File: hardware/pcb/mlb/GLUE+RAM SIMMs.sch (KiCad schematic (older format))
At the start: 15 parts

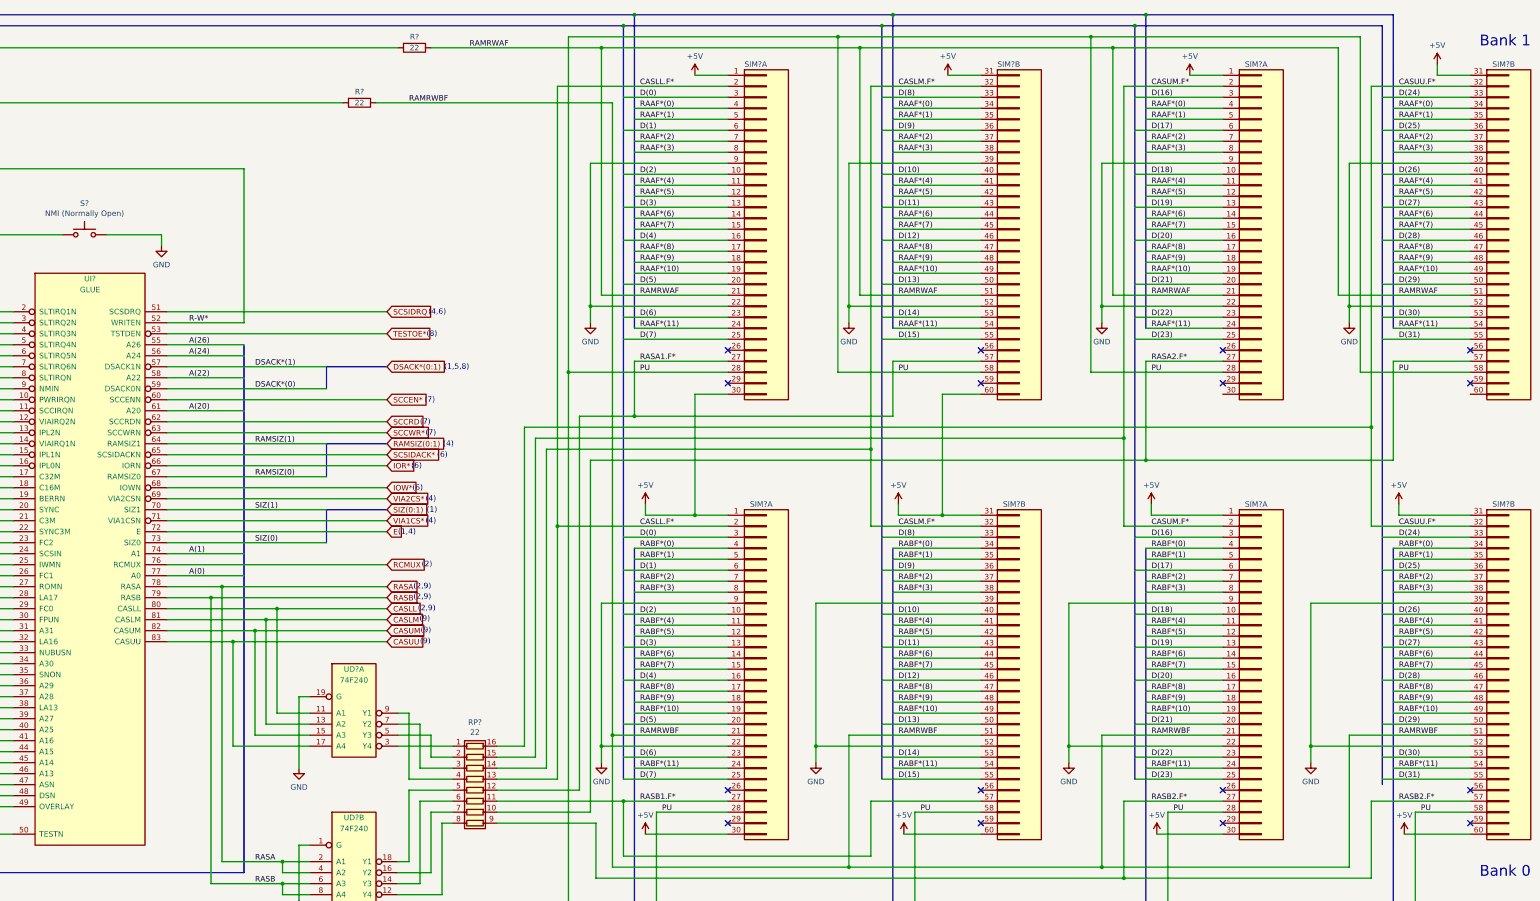
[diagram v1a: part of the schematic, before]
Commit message: Fix missing ground wires, fix some missing reference designators.
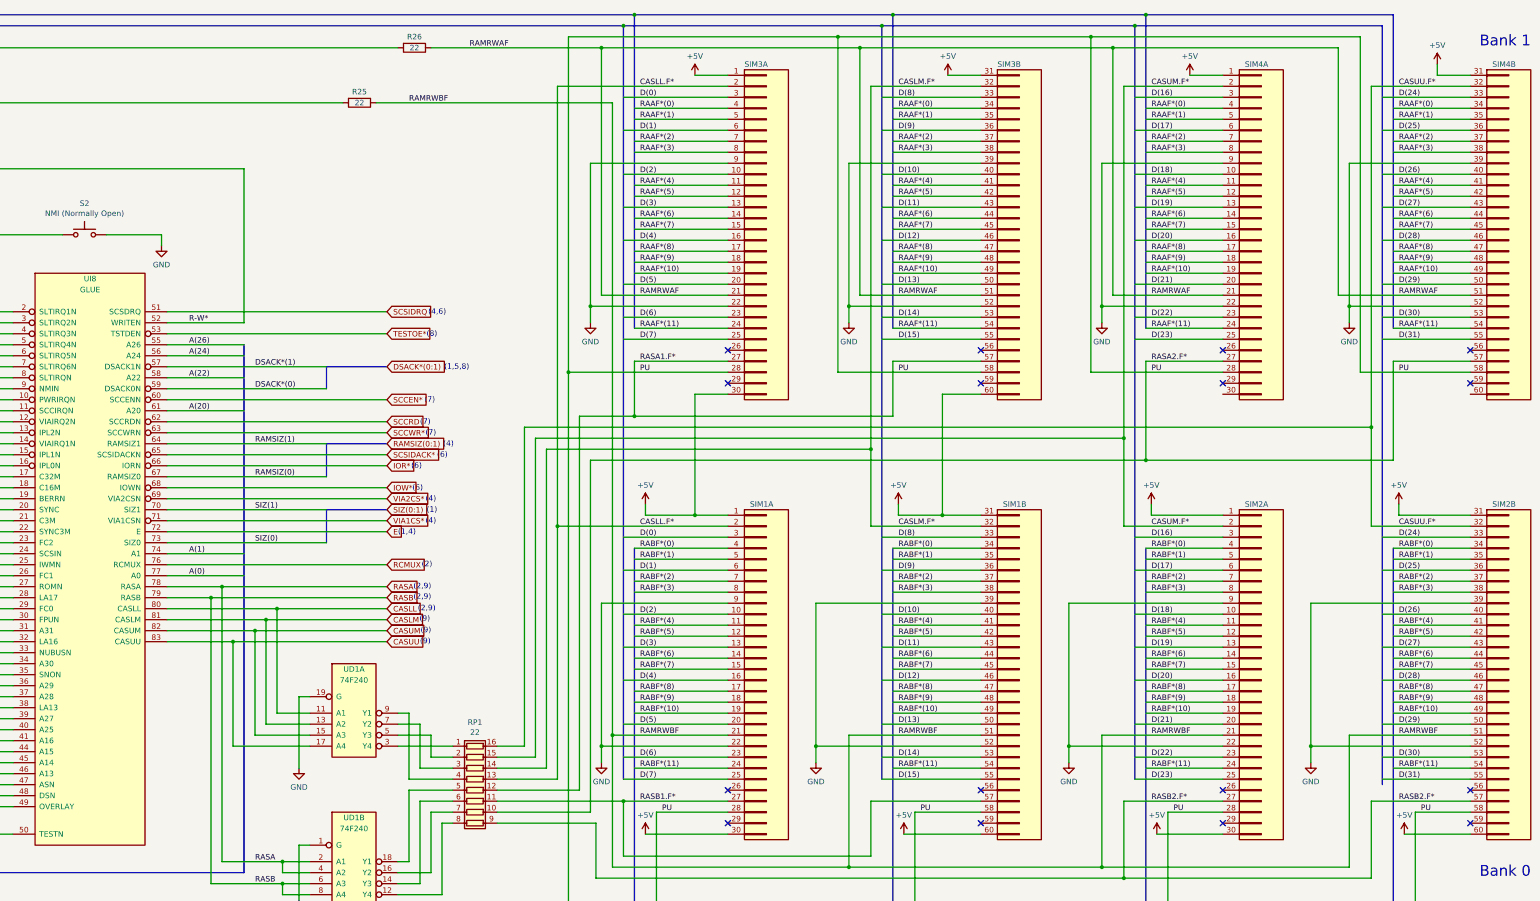
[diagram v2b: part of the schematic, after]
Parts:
- gave numbers to parts that had none: 10
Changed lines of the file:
@@
 $EndDescr
 $Comp
-L Device:R_Pack08 RP?
+L Device:R_Pack08 RP1
 U 1 1 5EBFAB6B
 P 6500 7700
-F 0 "RP?" V 5883 7700 50  0000 C CNN
+F 0 "RP1" V 5883 7700 50  0000 C CNN
 F 1 "22" V 5974 7700 50  0000 C CNN
 F 2 "" V 6975 7700 50  0001 C CNN
@@
 $EndComp
 $Comp
-L Macintosh_SE_30_Components:SIM SIM?
+L Macintosh_SE_30_Components:SIM SIM1
 U 1 1 5EC1F10E
 P 9000 6600
-F 0 "SIM?" H 9000 8100 50  0000 L CNN
+F 0 "SIM1" H 9000 8100 50  0000 L CNN
 F 1 "SIM" H 9100 8100 50  0001 C CNN
 F 2 "" H 8950 6650 50  0001 C CNN
@@
 $EndComp
 $Comp
-L Macintosh_SE_30_Components:SIM SIM?
+L Macintosh_SE_30_Components:SIM SIM1
 U 2 1 5EC1F118
 P 11300 6600
-F 0 "SIM?" H 11300 8100 50  0000 L CNN
+F 0 "SIM1" H 11300 8100 50  0000 L CNN
 F 1 "SIM" H 11400 8100 50  0001 C CNN
 F 2 "" H 11250 6650 50  0001 C CNN
@@
 $EndComp
 $Comp
-L Macintosh_SE_30_Components:SIM SIM?
+L Macintosh_SE_30_Components:SIM SIM2
 U 1 1 5EC1F122
 P 13500 6600
-F 0 "SIM?" H 13500 8100 50  0000 L CNN
+F 0 "SIM2" H 13500 8100 50  0000 L CNN
 F 1 "SIM" H 13600 8100 50  0001 C CNN
 F 2 "" H 13450 6650 50  0001 C CNN
@@
 $EndComp
 $Comp
-L Macintosh_SE_30_Components:SIM SIM?
+L Macintosh_SE_30_Components:SIM SIM2
 U 2 1 5EC1F12C
 P 15750 6600
-F 0 "SIM?" H 15750 8100 50  0000 L CNN
+F 0 "SIM2" H 15750 8100 50  0000 L CNN
 F 1 "SIM" H 15850 8100 50  0001 C CNN
 F 2 "" H 15700 6650 50  0001 C CNN
@@
 $EndComp
 $Comp
-L Macintosh_SE_30_Components:74F240 UD?
+L Macintosh_SE_30_Components:74F240 UD1
 U 1 1 5EC05118
 P 5400 6750
-F 0 "UD?" H 5400 6900 50  0000 C CNN
+F 0 "UD1" H 5400 6900 50  0000 C CNN
 F 1 "74F240" H 5400 6800 50  0000 C CNN
 F 2 "" H 5300 6900 50  0001 C CNN
@@
 $EndComp
 $Comp
-L Macintosh_SE_30_Components:74F240 UD?
+L Macintosh_SE_30_Components:74F240 UD1
 U 2 1 5EC06449
 P 5400 8100
-F 0 "UD?" H 5400 8250 50  0000 C CNN
+F 0 "UD1" H 5400 8250 50  0000 C CNN
 F 1 "74F240" H 5400 8150 50  0000 C CNN
 F 2 "" H 5300 8250 50  0001 C CNN
@@
 $EndComp
 $Comp
-L Macintosh_SE_30_Components:SIM SIM?
+L Macintosh_SE_30_Components:SIM SIM3
 U 1 1 5ECCAA30
 P 9000 2600
-F 0 "SIM?" H 8950 4100 50  0000 L CNN
+F 0 "SIM3" H 8950 4100 50  0000 L CNN
 F 1 "SIM" H 9100 4100 50  0001 C CNN
 F 2 "" H 8950 2650 50  0001 C CNN
@@
 $EndComp
 $Comp
-L Macintosh_SE_30_Components:SIM SIM?
+L Macintosh_SE_30_Components:SIM SIM3
 U 2 1 5ECCAA3A
 P 11300 2600
-F 0 "SIM?" H 11250 4100 50  0000 L CNN
+F 0 "SIM3" H 11250 4100 50  0000 L CNN
 F 1 "SIM" H 11400 4100 50  0001 C CNN
 F 2 "" H 11250 2650 50  0001 C CNN
@@
 $EndComp
 $Comp
-L Macintosh_SE_30_Components:SIM SIM?
+L Macintosh_SE_30_Components:SIM SIM4
 U 1 1 5ECCAA44
 P 13500 2600
-F 0 "SIM?" H 13500 4100 50  0000 L CNN
+F 0 "SIM4" H 13500 4100 50  0000 L CNN
 F 1 "SIM" H 13600 4100 50  0001 C CNN
 F 2 "" H 13450 2650 50  0001 C CNN
@@
 $EndComp
 $Comp
-L Macintosh_SE_30_Components:SIM SIM?
+L Macintosh_SE_30_Components:SIM SIM4
 U 2 1 5ECCAA4E
 P 15750 2600
-F 0 "SIM?" H 15750 4100 50  0000 L CNN
+F 0 "SIM4" H 15750 4100 50  0000 L CNN
 F 1 "SIM" H 15850 4100 50  0001 C CNN
 F 2 "" H 15700 2650 50  0001 C CNN
@@
 A(0:31)
 $Comp
-L Switch:SW_MEC_5G S?
+L Switch:SW_MEC_5G S2
 U 1 1 5EDD37E3
 P 2950 2650
-F 0 "S?" H 2950 2935 50  0000 C CNN
+F 0 "S2" H 2950 2935 50  0000 C CNN
 F 1 "NMI (Normally Open)" H 2950 2844 50  0000 C CNN
 F 2 "" H 2950 2850 50  0001 C CNN
@@
 $EndComp
 $Comp
-L Device:R R?
+L Device:R R25
 U 1 1 5F05E6F9
 P 5450 1450
-F 0 "R?" V 5350 1450 50  0000 C CNN
+F 0 "R25" V 5350 1450 50  0000 C CNN
 F 1 "22" V 5450 1450 50  0000 C CNN
 F 2 "" V 5380 1450 50  0001 C CNN
@@
 $EndComp
 $Comp
-L Device:R R?
+L Device:R R26
 U 1 1 6380CCE0
 P 5950 950
-F 0 "R?" V 5850 950 50  0000 C CNN
+F 0 "R26" V 5850 950 50  0000 C CNN
 F 1 "22" V 5950 950 50  0000 C CNN
 F 2 "" V 5880 950 50  0001 C CNN
@@
 	2300 4150 1200 4150
 $Comp
-L Macintosh_SE_30_Components:GLUE UI?
+L Macintosh_SE_30_Components:GLUE UI8
 U 1 1 5EBF6CFA
 P 2800 3100
-F 0 "UI?" H 3000 3150 50  0000 C CNN
+F 0 "UI8" H 3000 3150 50  0000 C CNN
 F 1 "GLUE" H 3000 3050 50  0000 C CNN
 F 2 "" H 2800 3100 50  0001 C CNN

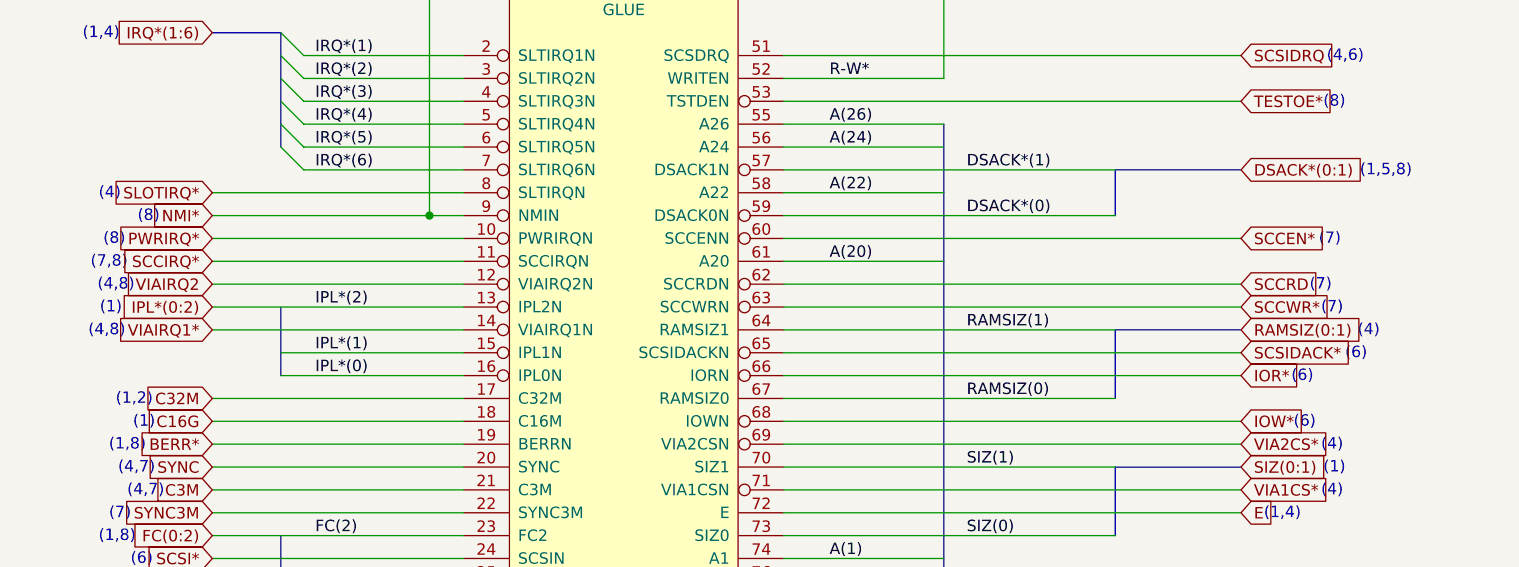
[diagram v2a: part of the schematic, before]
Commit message: Fix errors found in review of the Macintosh SE/30 schematic redraw.
Page 1:

* DSACK*(0:1) (syntax)
* R-W* (inconsistent syntax)
* IPL different syntax
* PDS 38, C16M not grounded
* PDS 39, should be grounded

Page 2:

* RAAF*(8), RABF*(9), RAAF*(10), RABF*(10) (syntax)
* RCMUX* (syntax)
* ROM* missing page 3 indicator
* ROMSIMM1 GND 10, 30, 64
* ROMSIMM1 Incorrect +5V lines
* ROMSIMM1 Confusing bus line drawing angles makes connections look
  duplicated

Page 3:

* VIAIRQ2* (syntax)
* VIAIRQ1N (syntax, on GLUE template)
* SCCRD* (syntax)

Page 4:

* VIA template, RS0, RS1, RS2, RS3 erroneously written as R50, R51,
  R52, R53
* V1PB7 erroneously written as VIPB7
* RTC-D erroneously written as RTC-O
* V1PA0, V1PA1, V1PA2 erroneously written as VIPA0, VIPA1, VIPA2
* warning: additional label BATT not present
* UL11 ADB template, P5 erroneously written as P2
* ADBO erroneously written as ADB0
* SNDINT* erroneously written as SNTINT*

Page 5:

* HSYNC* on UG7 (syntax)
* UJ6 confusing bus line makes signals look duplicated
* Video ROM UK6 not labeled with reference designator (already inside
  KiCad file, stale PDF?)
* VIDS4, VIDS3, VIDS2, VIDS1, VIDS0 erroneously written a VID54,
  VID53, VID53, VID51, VID50
* R-W* alternate page reference erroneously written as RW*
* 74F253 template, G erroneously labeled as GND
* 74F253 template, missing second G enable pin
* style: C0 in 74F253 template should not be C0(GND)
* warning: UA8 ALTVID line could have another label close to the chip

Page 6:

* warning: On SWIM, WRDATA could have label WR*
* DB25 connector: DP*, DB0*, DB1*, DB2*, DB3*, DB4*, DB5*, DB6*, DB7*
  (syntax)
* J8 Ribbon Connector: Missing +12V on 13, 15, 17, 19
* J6 DB-19: Missing +12V-DSK on 7, 8
* warning: missing RDDATA.F additional label near J6 DB-19 pin 18
* warning: missing WRITE.F additional label near J6 DB-19 pin 19
* warning: confusing bus line layout on 53C80 looks like duplicate
  wiring

Page 7:

* RXDA+ erroneously written as RXDB+
* HSKOA erroneo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
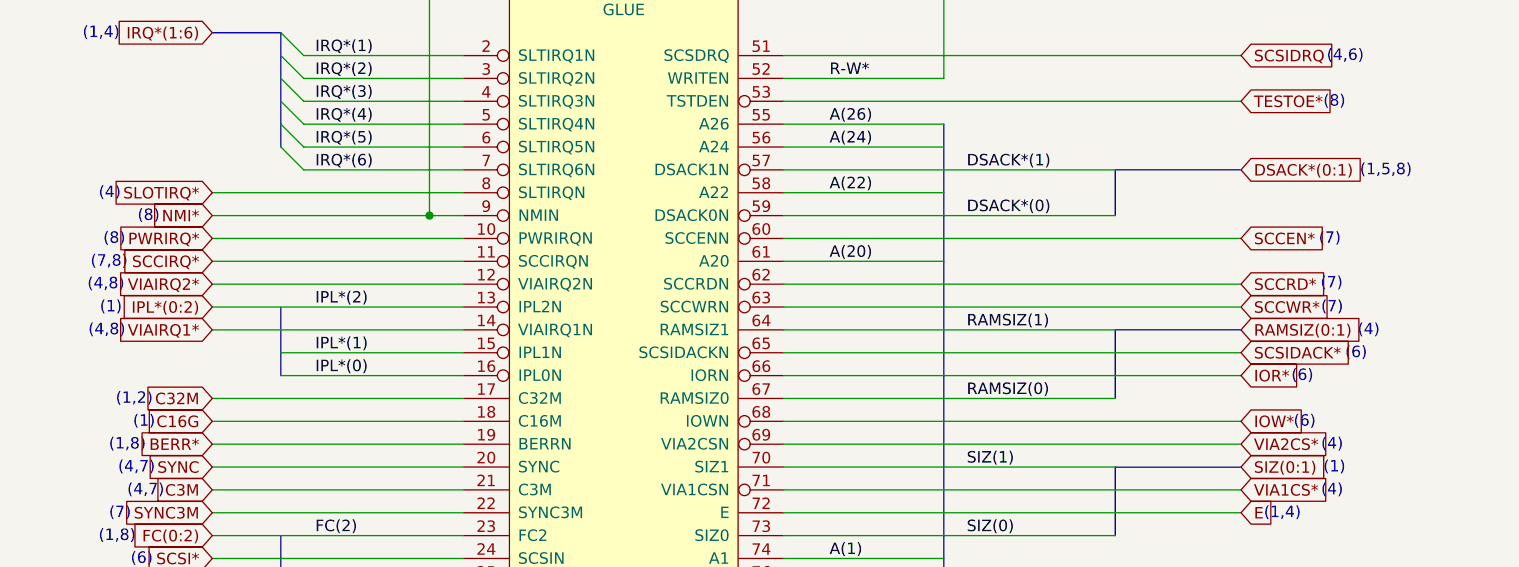
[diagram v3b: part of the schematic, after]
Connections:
- net labels added: SCCRD*, VIAIRQ2*
- net labels removed: SCCRD, VIAIRQ2
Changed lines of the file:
@@
 SCCIRQ*
 Text GLabel 1200 4350 0    50   Input ~ 0
-VIAIRQ2
+VIAIRQ2*
 Text GLabel 1200 4950 0    50   Input ~ 0
 C16G
@@
 SCCEN*
 Text GLabel 5700 4350 2    50   Input ~ 0
-SCCRD
+SCCRD*
 Text GLabel 5700 4450 2    50   Input ~ 0
 SCCWR*
@@
 U 1 1 5EBF6CFA
 P 2800 3100
+AR Path="/5EBF6CFA" Ref="UI8"  Part="1"
+AR Path="/5EC6E1BF/5EBF6CFA" Ref="UI8"  Part="1"
 F 0 "UI8" H 3000 3150 50  0000 C CNN
 F 1 "GLUE" H 3000 3050 50  0000 C CNN
@@
 Text Notes 830  4285 2    50   ~ 0
 (7,8)
-Text Notes 860  4385 2    50   ~ 0
+Text Notes 816  4384 2    50   ~ 0
 (4,8)
 Text Notes 805  4485 2    50   ~ 0
@@
 Text Notes 6040 4185 0    50   ~ 0
 (7)
-Text Notes 6000 4385 0    50   ~ 0
+Text Notes 6048 4380 0    50   ~ 0
 (7)
 Text Notes 6050 4485 0    50   ~ 0
